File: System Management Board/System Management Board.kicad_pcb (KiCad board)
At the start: 4 copper layers, 150 x 110 mm, 27 parts, among them J1 Conn_01x04_Male, J2 Conn_01x04_Male, J3 Conn_01x02_Male, J4 PJ-063BH, J5 Conn_01x02_Male, J6 Conn_02x06_Counter_Clockwise, J7 Conn_02x20_Odd_Even, K1 J115F11CH5VDCS61.5U, K2 J114FL1CS165VDC.41, K3 J114FL1CS165VDC.41, U1 SC0915, U2 OKI-78SR-5/1.5-W36E-C, U3 OKI-78SR-5/1.5-W36E-C, U4 NEO-M9N-00B

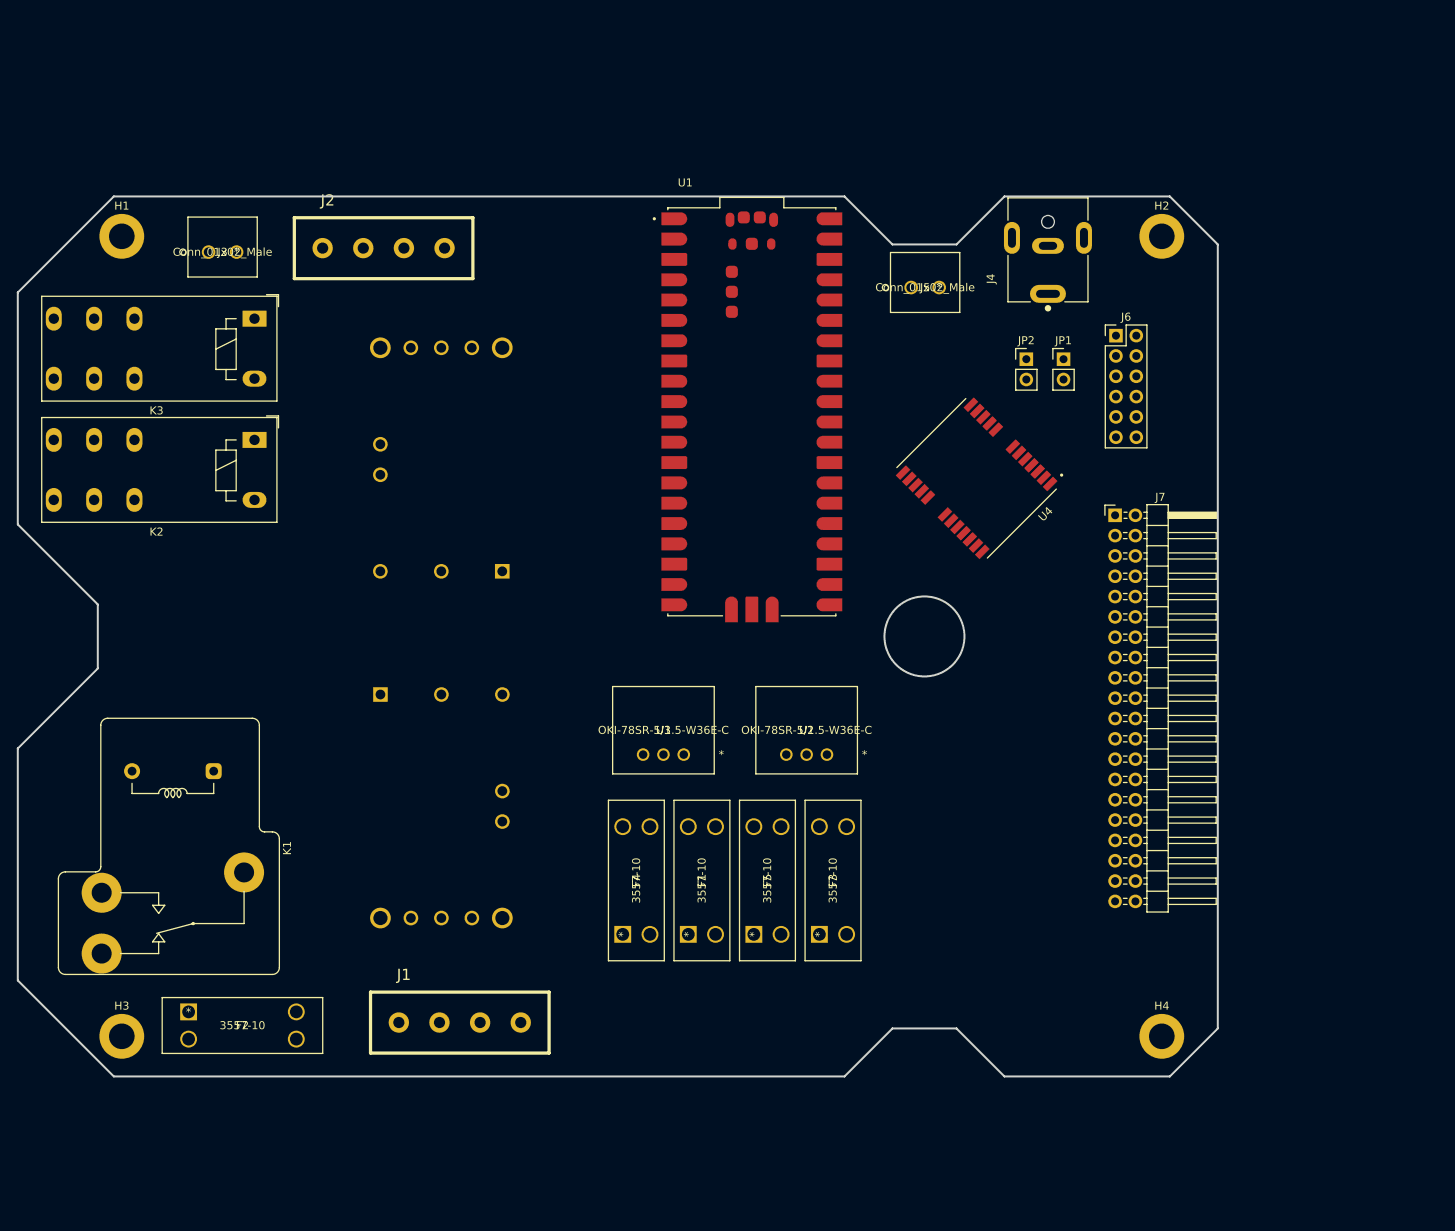
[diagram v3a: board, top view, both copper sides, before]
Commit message: Finished heatspreader and sent to Xometry, solidified postion of DC-DC converters and mounting holes on SMB PCB
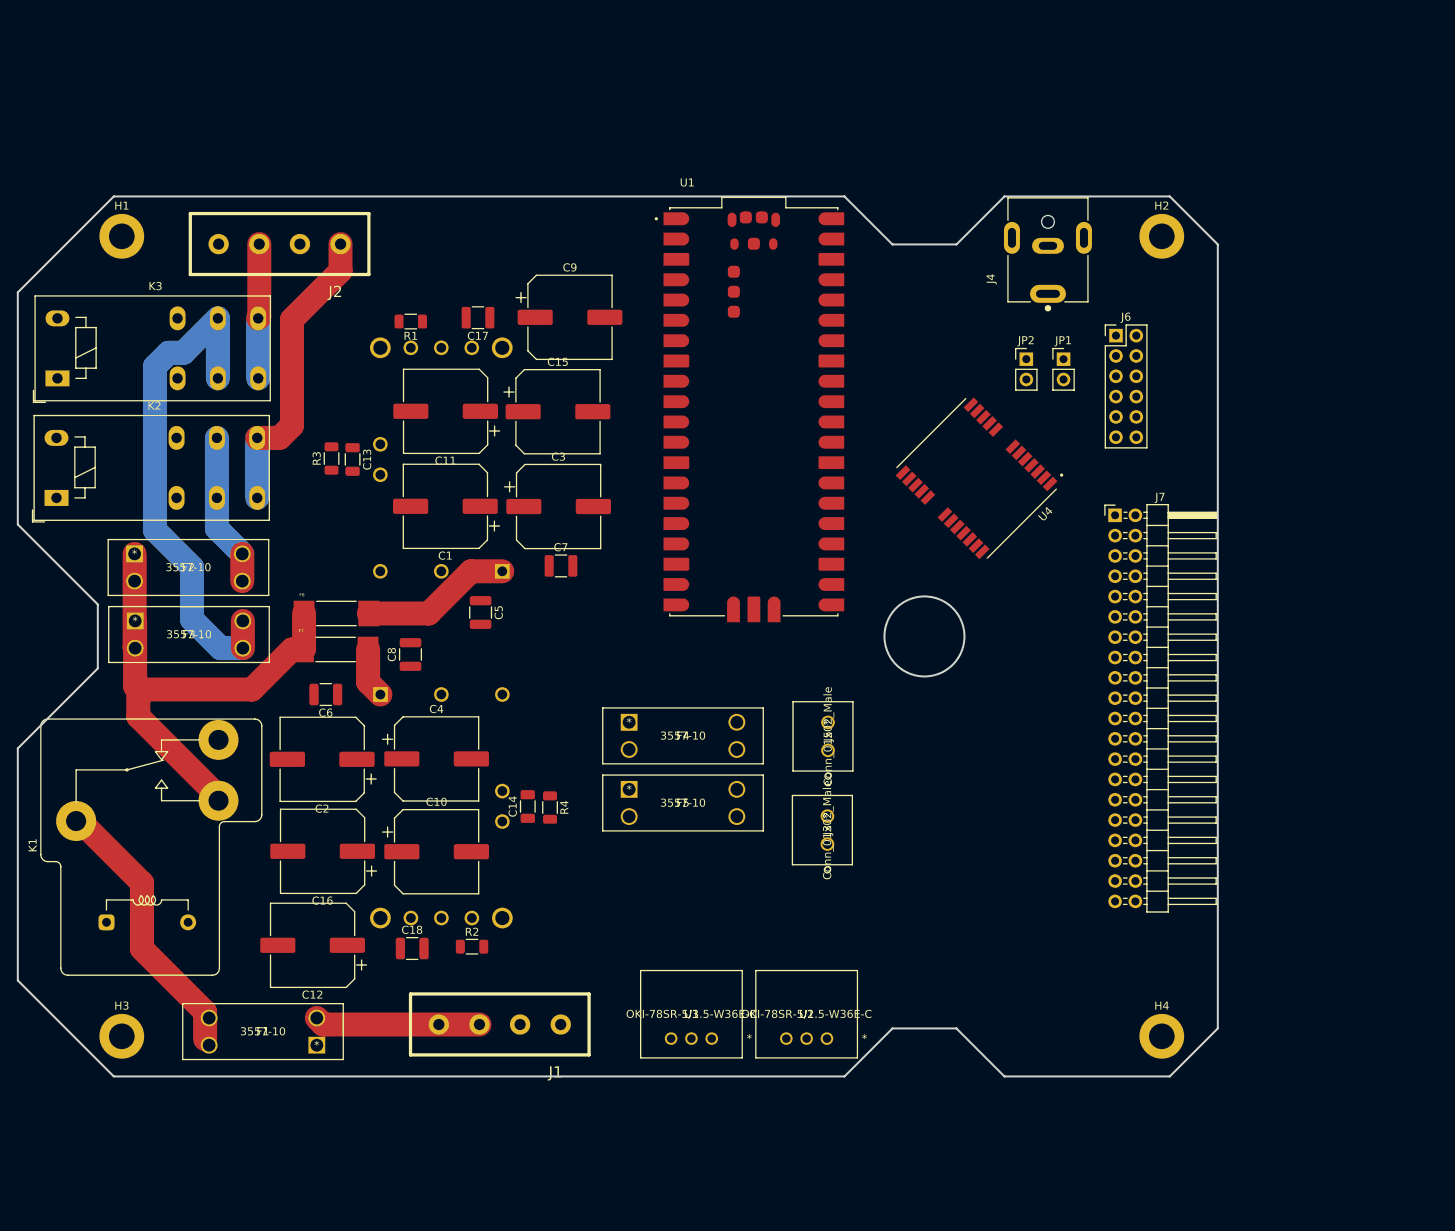
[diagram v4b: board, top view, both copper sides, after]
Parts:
- added C1: 270uF, Capacitor_SMD:CP_Elec_10x12.6, F.Cu at (127.2, 84.1)
- added C10: 100uF, Capacitor_SMD:CP_Elec_10x12.6, F.Cu at (126.1, 127.3)
- added C11: 100uF, Capacitor_SMD:CP_Elec_10x12.6, F.Cu at (127.2, 72.2)
- added C12: 100uF, Capacitor_SMD:CP_Elec_10x12.6, F.Cu at (110.6, 139.0)
- added C13: 0.1uF, Capacitor_SMD:C_1206_3216Metric, F.Cu at (115.6, 78.2)
- added C14: 0.1uF, Capacitor_SMD:C_1206_3216Metric, F.Cu at (137.5, 121.6)
- added C15: 100uF, Capacitor_SMD:CP_Elec_10x12.6, F.Cu at (141.2, 72.3)
- added C16: 100uF, Capacitor_SMD:CP_Elec_10x12.6, F.Cu at (111.8, 127.2)
- added C17: 0.1uF, Capacitor_SMD:C_1210_3225Metric, F.Cu at (131.2, 60.5)
- added C18: 0.1uF, Capacitor_SMD:C_1210_3225Metric, F.Cu at (123.0, 139.4)
- added C2: 270uF, Capacitor_SMD:CP_Elec_10x12.6, F.Cu at (111.8, 115.7)
- added C3: 270uF, Capacitor_SMD:CP_Elec_10x12.6, F.Cu at (141.3, 84.1)
- added C4: 270uF, Capacitor_SMD:CP_Elec_10x12.6, F.Cu at (126.1, 115.7)
- added C5: 10uF, Capacitor_SMD:C_1210_3225Metric, F.Cu at (131.6, 97.4)
- added C6: 10uF, Capacitor_SMD:C_1210_3225Metric, F.Cu at (112.2, 107.6)
- added C7: 10uF, Capacitor_SMD:C_1210_3225Metric, F.Cu at (141.6, 91.5)
- added C8: 10uF, Capacitor_SMD:C_1210_3225Metric, F.Cu at (122.8, 102.6)
- added C9: 100uF, Capacitor_SMD:CP_Elec_10x12.6, F.Cu at (142.8, 60.5)
- added F6: Fuse, SMB:FUSC9830X318N, F.Cu at (113.6, 97.5)
- added F7: Fuse, SMB:FUSC9830X318N, F.Cu at (113.5, 102.0)
- added R1: 4.64k, Resistor_SMD:R_1206_3216Metric, F.Cu at (122.8, 61.0)
- added R2: 28, Resistor_SMD:R_1206_3216Metric, F.Cu at (130.5, 139.1)
- added R3: 1k, Resistor_SMD:R_1206_3216Metric, F.Cu at (112.9, 78.1)
- added R4: 1k, Resistor_SMD:R_1206_3216Metric, F.Cu at (140.3, 121.8)
- moved J3 102.1 mm to (174.9, 122.8), turned to 90 degrees
- moved F3 94.1 mm to (88.4, 98.4), turned to 0 degrees
- moved F2 57.6 mm to (88.3, 90.0)
- moved J5 56.1 mm to (175.0, 111.1), turned to 90 degrees
- moved F1 48.5 mm to (111.1, 151.5), turned to 180 degrees
- moved U3 35.7 mm to (160.5, 150.6)
- moved U2 35.5 mm to (174.9, 150.6)
- moved F4 26.5 mm to (150.1, 111.1), turned to 0 degrees
- moved K2 26.3 mm to (78.3, 83.0), turned to 0 degrees
- moved K3 26.2 mm to (78.4, 68.1), turned to 0 degrees
- moved K1 24.2 mm to (89.9, 138.6), turned to 90 degrees
- moved F5 23.9 mm to (150.1, 119.5), turned to 0 degrees
- moved J2 13.0 mm to (106.5, 51.3), turned to 180 degrees
- moved J1 5.01 mm to (134.0, 148.9), turned to 180 degrees
- moved U1 0.25 mm to (165.7, 72.3)
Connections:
- F1 pad 1: unconnected-(F1-Pad1) -> /V_batt+
- F1 pad 2: unconnected-(F1-Pad2) -> /V_batt+
- F1 pad 3: unconnected-(F1-Pad3) -> /V_batt+ PROT
- F1 pad 4: unconnected-(F1-Pad4) -> /V_batt+ PROT
- F2 pad 1: unconnected-(F2-Pad1) -> /V_batt+ PROT SW
- F2 pad 2: unconnected-(F2-Pad2) -> /V_batt+ PROT SW
- F2 pad 3: unconnected-(F2-Pad3) -> /LIGHT BANK A PROT
- F2 pad 4: unconnected-(F2-Pad4) -> /LIGHT BANK A PROT
- F3 pad 1: unconnected-(F3-Pad1) -> /V_batt+ PROT SW
- F3 pad 2: unconnected-(F3-Pad2) -> /V_batt+ PROT SW
- F3 pad 3: unconnected-(F3-Pad3) -> /LIGHT BANK B PROT
- F3 pad 4: unconnected-(F3-Pad4) -> /LIGHT BANK B PROT
- F4 pad 1: unconnected-(F4-Pad1) -> /COMP PWR OUT
- F4 pad 2: unconnected-(F4-Pad2) -> /COMP PWR OUT
- F4 pad 3: unconnected-(F4-Pad3) -> /COMP PWR OUT PROT
- F4 pad 4: unconnected-(F4-Pad4) -> /COMP PWR OUT PROT
- F5 pad 1: unconnected-(F5-Pad1) -> /SWITCH PWR OUT
- F5 pad 2: unconnected-(F5-Pad2) -> /SWITCH PWR OUT
- F5 pad 3: unconnected-(F5-Pad3) -> /SWITCH PWR OUT PROT
- F5 pad 4: unconnected-(F5-Pad4) -> /SWITCH PWR OUT PROT
- J3 pad 2: SWITCH PWR OUT PROT -> /SWITCH PWR OUT PROT
- J4 pad 1: COMP PWR OUT PROT -> /COMP PWR OUT PROT
- J5 pad 1: COMP PWR OUT PROT -> /COMP PWR OUT PROT
- K1 pad 11: unconnected-(K1-Pad11) -> /V_batt+ PROT
- K1 pad 14: unconnected-(K1-Pad14) -> /V_batt+ PROT SW
- K2 pad 11: unconnected-(K2-Pad11) -> /LIGHT BANK A PROT
- K2 pad 14: unconnected-(K2-Pad14) -> /LIGHT BANK A PROT SW
- K3 pad 11: unconnected-(K3-Pad11) -> /LIGHT BANK B PROT
- K3 pad 14: unconnected-(K3-Pad14) -> /LIGHT BANK B PROT SW
- PS1 pad 1: unconnected-(PS1-Pad1) -> /CPS_IN_PROT
- PS1 pad 2: unconnected-(PS1-Pad2) -> /~{COMP PWR EN}
- PS1 pad 3: unconnected-(PS1-Pad3) -> GND
- PS1 pad 32: unconnected-(PS1-Pad32) -> GND
- PS1 pad 34: unconnected-(PS1-Pad34) -> Net-(C13-Pad1)
- PS1 pad 4: unconnected-(PS1-Pad4) -> GND
- PS1 pad 5: unconnected-(PS1-Pad5) -> /COMP PWR GOOD
- PS1 pad 6: unconnected-(PS1-Pad6) -> Net-(PS1-Pad6)
- PS1 pad 7: unconnected-(PS1-Pad7) -> /COMP PWR OUT
- PS1 pad 8: unconnected-(PS1-Pad8) -> /COMP PWR OUT
- PS2 pad 1: unconnected-(PS2-Pad1) -> /PSPS_IN_PROT
- PS2 pad 2: unconnected-(PS2-Pad2) -> /~{SWITCH PWR EN}
- PS2 pad 3: unconnected-(PS2-Pad3) -> GND
- PS2 pad 32: unconnected-(PS2-Pad32) -> GND
- PS2 pad 34: unconnected-(PS2-Pad34) -> Net-(C14-Pad1)
- PS2 pad 4: unconnected-(PS2-Pad4) -> GND
- PS2 pad 5: unconnected-(PS2-Pad5) -> /SWITCH PWR GOOD
- PS2 pad 6: unconnected-(PS2-Pad6) -> Net-(PS2-Pad6)
- PS2 pad 7: unconnected-(PS2-Pad7) -> /SWITCH PWR OUT
- PS2 pad 8: unconnected-(PS2-Pad8) -> /SWITCH PWR OUT
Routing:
- net /V_batt+ PROT SW: track 0.00 -> 65.3 mm
- net /LIGHT BANK B PROT: track 0.00 -> 62.6 mm
- net /LIGHT BANK A PROT SW: track 0.00 -> 37.7 mm
- net /V_batt+ PROT: track 0.00 -> 34.5 mm
- net /V_batt+: track 0.00 -> 20.7 mm
- net /LIGHT BANK A PROT: track 0.00 -> 19.2 mm
- net /CPS_IN_PROT: track 0.00 -> 18.9 mm
- net /LIGHT BANK B PROT SW: track 0.00 -> 16.8 mm
- net /PSPS_IN_PROT: track 0.00 -> 6.27 mm

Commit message: Added aux outputs and worked on routing for high current traces
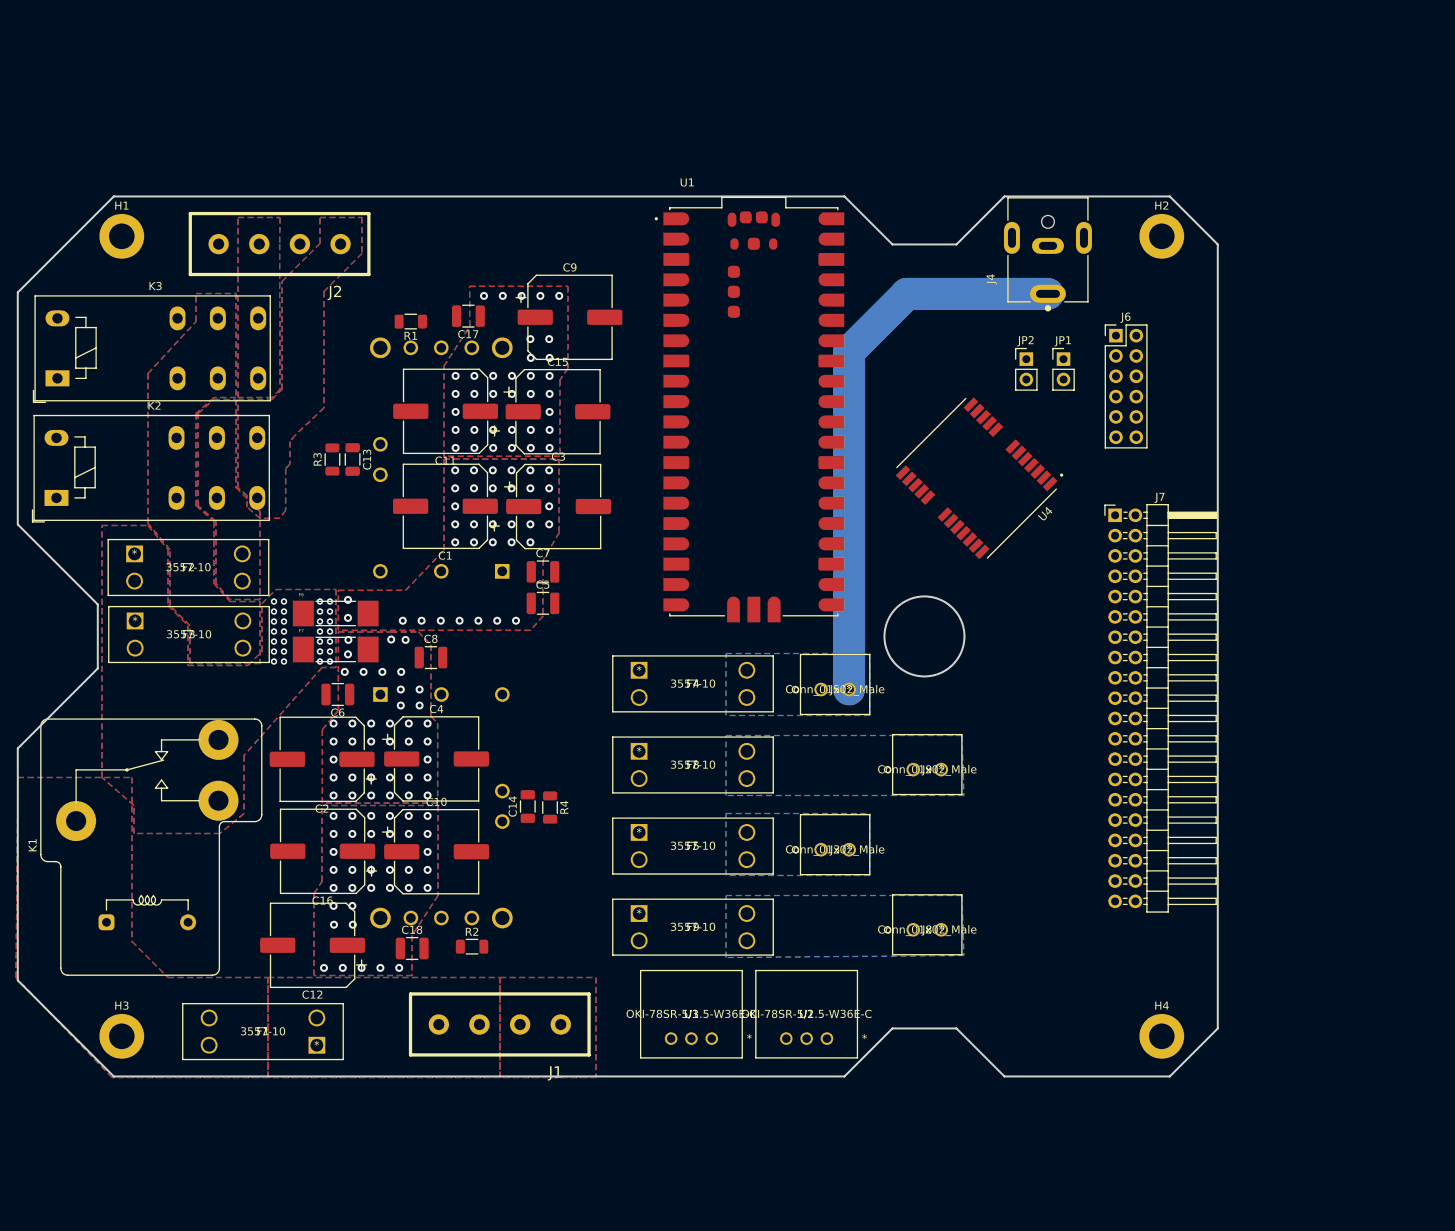
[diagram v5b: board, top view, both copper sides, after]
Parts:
- added F8: 3557-10, SMB:3557-10, F.Cu at (151.4, 114.7)
- added F9: 3557-10, SMB:3557-10, F.Cu at (151.4, 135.0)
- added J8: Conn_01x02_Male, SMB:1843606, F.Cu at (189.2, 137.0)
- added J9: Conn_01x02_Male, SMB:1843606, F.Cu at (189.2, 117.0)
- moved C5 7.88 mm to (139.4, 96.2), turned to 0 degrees
- moved F4 6.62 mm to (151.4, 104.6)
- moved F5 5.53 mm to (151.4, 124.9)
- moved J3 5.00 mm to (177.6, 127.0), turned to 0 degrees
- moved J5 4.88 mm to (177.6, 107.0), turned to 0 degrees
- moved C8 2.59 mm to (125.4, 103.0), turned to 0 degrees
- moved C7 2.37 mm to (139.4, 92.3)
- moved C6 1.50 mm to (113.7, 107.6)
- moved C17 1.22 mm to (130.1, 60.3)
- moved R3 0.16 mm to (113.1, 78.2)
- moved F6 0.09 mm to (113.5, 97.5)
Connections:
- net /COMP PWR OUT renamed /15v PWR
- net /SWITCH PWR OUT renamed /48V PWR
- J5 pad 1: /COMP PWR OUT PROT -> GND
- J5 pad 2: GND -> /COMP PWR OUT PROT
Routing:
- net /COMP PWR OUT PROT: track 0.00 -> 70.1 mm
- net /V_batt+ PROT SW: track 65.3 -> 0.00 mm, vias 0 -> 28
- net /LIGHT BANK B PROT: track 62.6 -> 0.00 mm
- net /LIGHT BANK A PROT SW: track 37.7 -> 0.00 mm
- net /V_batt+ PROT: track 34.5 -> 0.00 mm
- net /V_batt+: track 20.7 -> 0.00 mm
- net /LIGHT BANK A PROT: track 19.2 -> 0.00 mm
- net /CPS_IN_PROT: track 18.9 -> 0.00 mm, vias 0 -> 34
- net /LIGHT BANK B PROT SW: track 16.8 -> 0.00 mm
- net /PSPS_IN_PROT: track 6.27 -> 0.00 mm, vias 0 -> 38
- net /48V PWR: vias 0 -> 35
- net /15v PWR: vias 0 -> 35
- added copper zone on B.Cu, net /15V Aux PWR OUT PROT
- added copper zone on B.Cu, net /15v PWR
- added copper zone on F.Cu, net /15v PWR
- added copper zone on In2.Cu, net /15v PWR
- added copper zone on B.Cu, net /48V Aux PWR OUT PROT
- added copper zone on B.Cu, net /48V PWR
- added copper zone on F.Cu, net /48V PWR
- added copper zone on In2.Cu, net /48V PWR
- added copper zone on B.Cu, net /COMP PWR OUT PROT
- added copper zone on B.Cu, net /CPS_IN_PROT
- added copper zone on F.Cu, net /CPS_IN_PROT
- added copper zone on In2.Cu, net /CPS_IN_PROT
- added copper zone on B.Cu, net /LIGHT BANK A PROT
- added copper zone on F.Cu, net /LIGHT BANK A PROT
- added copper zone on B.Cu, net /LIGHT BANK A PROT SW
- added copper zone on F.Cu, net /LIGHT BANK A PROT SW
- added copper zone on B.Cu, net /LIGHT BANK B PROT
- added copper zone on F.Cu, net /LIGHT BANK B PROT
- added copper zone on B.Cu, net /LIGHT BANK B PROT SW
- added copper zone on F.Cu, net /LIGHT BANK B PROT SW
- added copper zone on B.Cu, net /PSPS_IN_PROT
- added copper zone on F.Cu, net /PSPS_IN_PROT
- added copper zone on In2.Cu, net /PSPS_IN_PROT
- added copper zone on B.Cu, net /SWITCH PWR OUT PROT
- added copper zone on B.Cu, net /V_batt+
- added copper zone on F.Cu, net /V_batt+
- added copper zone on In2.Cu, net /V_batt+
- added copper zone on B.Cu, net /V_batt+ PROT
- added copper zone on F.Cu, net /V_batt+ PROT
- added copper zone on In2.Cu, net /V_batt+ PROT
- added copper zone on B.Cu, net /V_batt+ PROT SW
- added copper zone on F.Cu, net /V_batt+ PROT SW
- added copper zone on In2.Cu, net /V_batt+ PROT SW
- added copper zone on B.Cu, net GND
- added copper zone on F.Cu, net GND
- added copper zone on In2.Cu, net GND
